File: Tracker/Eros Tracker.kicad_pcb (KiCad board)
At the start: 4 copper layers, 50 x 50 mm, 57 parts, among them J1 2171790001, J2 S8B-PH-SM4-TB(LF)(SN), J3 S2B-PH-SM4-TB(LF)(SN), J4 24881, J5 24881, J6 24881, J7 24881, M1 Motor_DC, Q1 NX138BKSX, Q2 NX138BKSX, Q3 DMP31D7LDW-7, Q4 DMP2240UDM-7, Q5 DMC1028UVT-7, Q6 DMC1028UVT-7, SW1 EVQ-P7A01P, U1 ESP32-C3-WROOM-02-N4, U2 TPS62A01A, U3 MCP73834-FCI/MF, U4 BNO086

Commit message: Alpha release
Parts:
- added G***: LOGO, LOGO, B.Cu at (164.9, 104.4)
- moved C3 67.0 mm to (179.1, 109.5), turned to 180 degrees
- moved R13 66.8 mm to (179.1, 114.7), turned to 180 degrees
- moved L1 66.5 mm to (179.0, 112.2), turned to 0 degrees
- moved C2 60.0 mm to (175.6, 109.5), turned to 0 degrees
- moved R14 59.6 mm to (175.5, 114.7), turned to 180 degrees
- moved U2 59.5 mm to (175.5, 112.2), turned to -90 degrees
- moved SW1 45.8 mm to (187.7, 94.6), turned to -90 degrees
- moved J1 42.0 mm to (186.0, 106.5), turned to 90 degrees
- moved R3 38.3 mm to (184.2, 98.6), turned to 180 degrees
- moved J3 36.0 mm to (147.0, 96.5)
- moved Q3 34.5 mm to (183.5, 95.6), turned to 90 degrees
- moved Q2 31.6 mm to (180.5, 95.6), turned to 90 degrees
- moved R23 30.2 mm to (180.0, 104.2), turned to 180 degrees
- moved R5 29.2 mm to (178.0, 95.6), turned to -90 degrees
- moved R22 29.2 mm to (179.0, 107.5), turned to 180 degrees
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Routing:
- net +BATT: track 6.89 -> 112.1 mm, vias 0 -> 4
- net Net-(LED1-A): track 0.00 -> 91.3 mm
- net /Eros Tracker Connectors/POWER_VIN1: track 0.00 -> 72.2 mm, vias 0 -> 4
- net /Eros Tracker BNO086 IMU/~{RESET}: track 0.00 -> 70.5 mm, vias 0 -> 4
- net GND: track 4.89 -> 67.5 mm, vias 1 -> 29
- net /Eros Tracker Connectors/VBUS: track 8.37 -> 67.6 mm, vias 0 -> 5
- net /Eros Tracker Connectors/POWER_VIN2: track 0.00 -> 58.8 mm, vias 0 -> 2
- net /Eros Tracker Power & Battery/~{BAT_STAT_CHARGING}: track 2.19 -> 42.0 mm, vias 0 -> 2
- net /Eros Tracker BNO086 IMU/I2C_SCL: track 3.34 -> 41.5 mm, vias 0 -> 2
- net /Eros Tracker Microcontroller/TACT_MOTOR0: track 0.00 -> 34.1 mm, vias 0 -> 2
- net /Eros Tracker Connectors/INT: track 0.00 -> 30.4 mm, vias 0 -> 2
- net /Eros Tracker BNO086 IMU/I2C_SDA: track 3.34 -> 33.3 mm, vias 0 -> 2
- net +3V3: track 10.3 -> 36.7 mm, vias 3 -> 14
- net /Eros Tracker Microcontroller/ENABLE_LATCH: track 0.00 -> 26.0 mm, vias 0 -> 2
- net /Eros Tracker Microcontroller/TACT_MOTOR1: track 3.67 -> 27.8 mm, vias 0 -> 2
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- added copper zone on In2.Cu, net +3V3
- added copper zone on In1.Cu, net GND
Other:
- board text added: "0"
- board text added: "0 mm"
- board text added: "0.01 mm"
- board text added: "0.02"
- board text added: "0.035 mm"
- board text added: "0.0900 mm / 0.0900 mm"
- board text added: "0.1 mm"
- board text added: "0.2500 mm"
- board text added: "1"
- board text added: "1.64 mm"
- board text added: "2.0000 mm"
- board text added: "3.3"
- board text added: "4"
- board text added: "4.5"
- board text added: "50.0000 mm x 50.0000 mm"
- board text added: "B.Cu"
- board text added: "B.Mask"
- board text added: "B.Paste"
- board text added: "B.Silkscreen"
- board text added: "BOARD CHARACTERISTICS"
- board text added: "Board Thickness:"
- board text added: "Board overall dimensions:"
- board text added: "Bottom Silk Screen"
- board text added: "Bottom Solder Mask"
- board text added: "Bottom Solder Paste"
- board text added: "Castellated pads:"
- board text added: "Color"
- board text added: "Copper Finish:"
- board text added: "Copper Layer Count:"
- board text added: "Dielectric 1"
- board text added: "Dielectric 2"
- board text added: "Dielectric 3"
- board text added: "Edge card connectors:"
- board text added: "Epsilon R"
- board text added: "F.Cu"
- board text added: "F.Mask"
- board text added: "F.Paste"
- board text added: "F.Silkscreen"
- board text added: "FR4"
- board text added: "Impedance Control:"
- board text added: "In1.Cu"
- board text added: "In2.Cu"
- board text added: "JLCJLCJLCJLC"
- board text added: "Layer Name"
- board text added: "Loss Tangent"
- board text added: "Material"
- board text added: "Min hole diameter:"
- board text added: "Min track/spacing:"
- board text added: "No"
- board text added: "None"
- board text added: "Not specified"
- board text added: "Plated Board Edge:"
- board text added: "Thickness (mm)"
- board text added: "Top Silk Screen"
- board text added: "Top Solder Mask"
- board text added: "Top Solder Paste"
- board text added: "Type"
- board text added: "copper"
- board text added: "core"
- board text added: "prepreg"

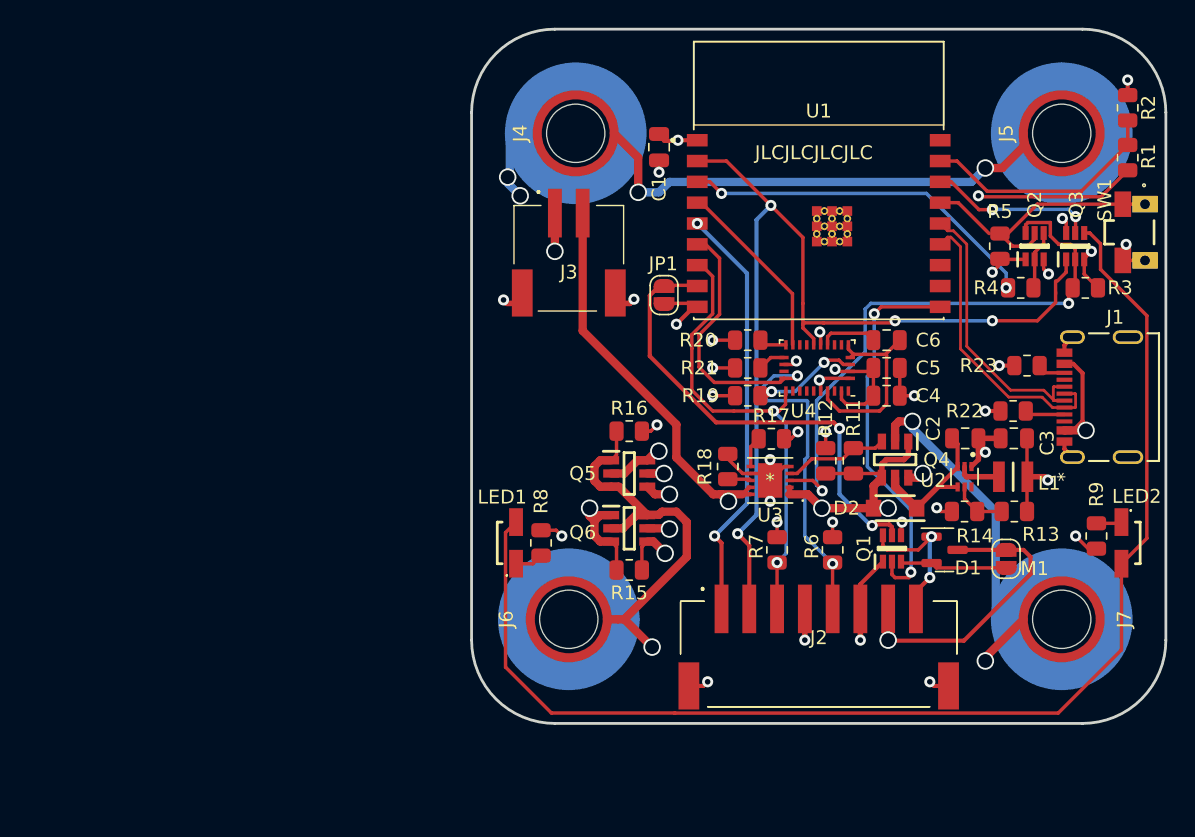
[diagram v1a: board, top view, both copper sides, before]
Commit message: RevC release. Power passthrough, battery voltage monitoring, IMU interrupt line fixed. TVS diodes added to all human-reachable connections.
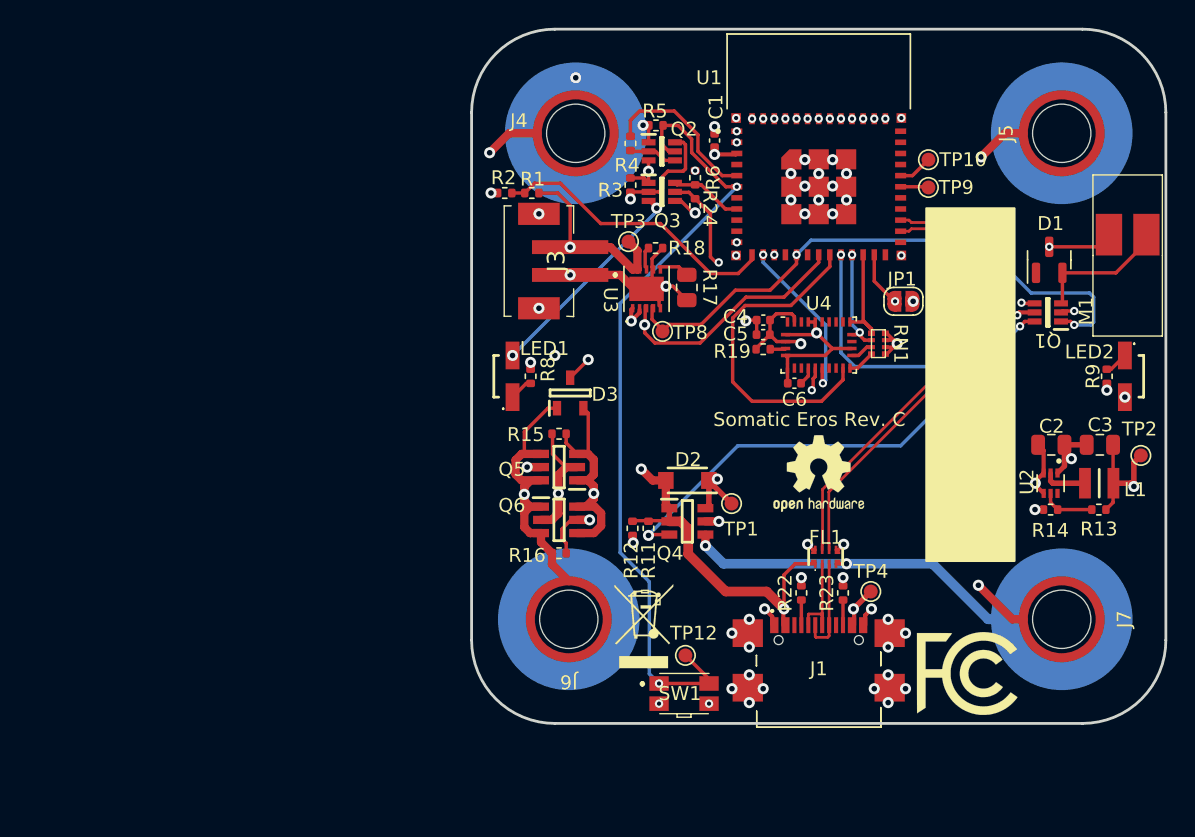
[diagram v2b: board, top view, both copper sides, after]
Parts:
- removed J2: S8B-PH-SM4-TB(LF)(SN), Eros Tracker:S8BPHSM4TBLFSN
- removed R20, R21, R7: 2.2k, Resistor_SMD:R_0805_2012Metric
- added D3: PESD5V2S2UT,215, Eros Tracker:SOT95P230X110-3N, F.Cu at (147.1, 106.2)
- added FL1: ECMF02-4CMX8, Eros Tracker:ECMF024CMX8, F.Cu at (165.5, 118.0)
- added R24: 10k 1%, Resistor_SMD:R_0402_1005Metric, F.Cu at (156.1, 92.7)
- added REF**: FCC-Logo_7.3x6mm_SilkScreen, Symbol:FCC-Logo_7.3x6mm_SilkScreen, F.Cu at (175.7, 126.4)
- added REF**: WEEE-Logo_4.2x6mm_SilkScreen, Symbol:WEEE-Logo_4.2x6mm_SilkScreen, F.Cu at (152.4, 123.0)
- added REF**: OSHW-Logo2_7.3x6mm_SilkScreen, Symbol:OSHW-Logo2_7.3x6mm_SilkScreen, F.Cu at (165.0, 112.0)
- added RN1: 2.2k, Eros Tracker:CAY10-xxxJ4, F.Cu at (169.3, 102.7)
- added TP1: TestPoint, TestPoint:TestPoint_Pad_D1.0mm, F.Cu at (158.7, 114.2)
- added TP10: TestPoint, TestPoint:TestPoint_Pad_D1.0mm, F.Cu at (172.9, 89.4)
- added TP12: TestPoint, TestPoint:TestPoint_Pad_D1.0mm, F.Cu at (155.4, 125.1)
- added TP2: TestPoint, TestPoint:TestPoint_Pad_D1.0mm, F.Cu at (188.2, 110.7)
- added TP3: TestPoint, TestPoint:TestPoint_Pad_D1.0mm, F.Cu at (151.3, 95.3)
- added TP4: TestPoint, TestPoint:TestPoint_Pad_D1.0mm, F.Cu at (168.8, 120.5)
- added TP8: TestPoint, TestPoint:TestPoint_Pad_D1.0mm, F.Cu at (153.8, 101.8)
- added TP9: TestPoint, TestPoint:TestPoint_Pad_D1.0mm, F.Cu at (172.9, 91.4)
- C1, C4, C5, C6: footprint Capacitor_SMD:C_0805_2012Metric -> Capacitor_SMD:C_0402_1005Metric
- J1: value 2171790001 -> USB4110-GF-A; footprint Eros Tracker:2171790001_MOL -> Eros Tracker:USB4110GFA
- J3: value S2B-PH-SM4-TB(LF)(SN) -> B2B-PH-SM4-TB(LF)(SN); footprint Eros Tracker:S2BPHSM4TBLFSN -> Eros Tracker:B2BPHSM4TBLFSN
- LOGO: renamed from G***; footprint LOGO -> Eros Tracker:SomaticLogo
- M1: value Motor_DC -> LCM04084521-B1; footprint Jumper:SolderJumper-2_P1.3mm_Open_RoundedPad1.0x1.5mm -> Eros Tracker:LCM04084521-B1
- R1, R11, R12, R13, R14, R15, R16, R18, R19, R2, R22, R23, R3, R4, R5, R8, R9: footprint Resistor_SMD:R_0805_2012Metric -> Resistor_SMD:R_0402_1005Metric
- R6: value 2.2k -> 100k; footprint Resistor_SMD:R_0805_2012Metric -> Resistor_SMD:R_0402_1005Metric
- SW1: footprint Eros Tracker:EVQ-9P701P -> Eros Tracker:EVQ-P7J01P
- U1: value ESP32-C3-WROOM-02-N4 -> ESP32-C3-MINI-1-N4; footprint Eros Tracker:ESP32-C3-WROOM-02-N4-MODULE_ESP32-C3-WROOM-02-H4 -> Eros Tracker:XCVR_ESP32-C3-MINI-1-N4
- moved SW1 46.6 mm to (155.0, 127.8), turned to 0 degrees
- moved R2 45.3 mm to (142.4, 91.8), turned to 180 degrees
- moved R1 43.0 mm to (144.3, 91.8), turned to 180 degrees
- moved R3 33.6 mm to (151.4, 91.2), turned to -90 degrees
- moved Q3 30.0 mm to (153.7, 91.7), turned to 0 degrees
- moved R4 30.0 mm to (151.4, 88.2), turned to -90 degrees
- moved J1 29.1 mm to (165.0, 126.6), turned to 0 degrees
- moved R6 28.6 mm to (156.1, 90.7), turned to 90 degrees
- moved Q2 27.7 mm to (153.7, 88.8), turned to 0 degrees
- moved R5 26.3 mm to (153.3, 86.9), turned to 180 degrees
- moved M1 23.5 mm to (187.2, 96.3), turned to 90 degrees
- moved D1 22.2 mm to (181.6, 96.6), turned to 90 degrees
- moved R23 21.1 mm to (166.8, 120.6), turned to 90 degrees
- moved Q1 20.4 mm to (181.5, 100.4), turned to 180 degrees
- moved R22 20.1 mm to (163.8, 120.6), turned to 90 degrees
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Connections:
- C6 pad 2: Net-(U4-PS0/WAKE) -> GND
- D1 pad 1: /Eros Tracker Connectors/-EXT_MOTOR -> unconnected-(D1-Pad1)
- J1 pad A6: /Eros Tracker Connectors/USB_D+ -> Net-(FL1-D+_1)
- J1 pad A7: /Eros Tracker Connectors/USB_D- -> Net-(FL1-D-_1)
- J1 pad B6: /Eros Tracker Connectors/USB_D+ -> Net-(FL1-D+_1)
- J1 pad B7: /Eros Tracker Connectors/USB_D- -> Net-(FL1-D-_1)
- JP1 pad 2: /Eros Tracker Microcontroller/TACT_MOTOR0 -> /Eros Tracker Microcontroller/~{LED}
- Q1 pad 1: GND -> /Eros Tracker Microcontroller/~{BAT_STAT_CHRG_DONE}
- Q1 pad 2: /Eros Tracker Microcontroller/TACT_MOTOR1 -> +3V3
- Q1 pad 5: /Eros Tracker Microcontroller/TACT_MOTOR0 -> /Eros Tracker Microcontroller/TACT_MOTOR
- Q1 pad 6: /Eros Tracker Connectors/-EXT_MOTOR -> Net-(Q1A-D1)
- Q2 pad 6: /Eros Tracker Power & Battery/~{BAT_STAT_CHARGING} -> /Eros Tracker Microcontroller/~{BAT_STAT_CHARGING}
- Q3 pad 1: /Eros Tracker BNO086 IMU/~{RESET} -> +3V3
- Q3 pad 2: /Eros Tracker Power & Battery/~{BAT_STAT_CHARGING} -> /Eros Tracker Microcontroller/~{BAT_STAT_CHARGING}
- Q3 pad 3: +3V3 -> Net-(LED1-A)
- Q3 pad 4: Net-(LED1-A) -> +3V3
- Q3 pad 6: +3V3 -> /Eros Tracker Microcontroller/MCU_ENABLE
- Q4 pad 2: /Eros Tracker Connectors/VBUS_OUT -> /Eros Tracker Connectors/VBUS
- Q4 pad 3: /Eros Tracker Power & Battery/~{BAT_STAT_CHRG_DONE} -> Net-(Q1A-D1)
- Q4 pad 4: /Eros Tracker Connectors/VBUS -> /Eros Tracker Connectors/VBUS_OUT
- Q4 pad 5: /Eros Tracker Power & Battery/VIN -> +BATT
- Q4 pad 6: +BATT -> /Eros Tracker Power & Battery/VIN
- Q5 pad 2: /Eros Tracker Connectors/POWER_VIN1 -> /Eros Tracker Connectors/VBUS
- Q5 pad 4: /Eros Tracker Connectors/VBUS -> /Eros Tracker Connectors/POWER_VIN1
- Q6 pad 2: /Eros Tracker Connectors/POWER_VIN2 -> /Eros Tracker Connectors/VBUS
- Q6 pad 4: /Eros Tracker Connectors/VBUS -> /Eros Tracker Connectors/POWER_VIN2
- R1 pad 2: Net-(U1-IO1) -> /Eros Tracker Microcontroller/ADC_BATT_V
- R11 pad 2: /Eros Tracker Power & Battery/~{BAT_STAT_CHRG_DONE} -> Net-(Q1A-D1)
- R2 pad 1: Net-(U1-IO1) -> /Eros Tracker Microcontroller/ADC_BATT_V
- R3 pad 2: /Eros Tracker Power & Battery/~{BAT_STAT_CHARGING} -> /Eros Tracker Microcontroller/~{BAT_STAT_CHARGING}
- R6 pad 1: +3V3 -> /Eros Tracker Microcontroller/MCU_ENABLE
- R6 pad 2: /Eros Tracker BNO086 IMU/I2C_SCL -> GND
- U1 pad 1: +3V3 -> GND
- U1 pad 10: /Eros Tracker Microcontroller/TACT_MOTOR1 -> unconnected-(U1-NC-Pad10)
- U1 pad 11: unconnected-(U1-RXD-Pad11) -> GND
- U1 pad 12: unconnected-(U1-TXD-Pad12) -> /Eros Tracker Microcontroller/ADC_BATT_V
- U1 pad 13: /Eros Tracker Connectors/USB_D- -> /Eros Tracker BNO086 IMU/~{RESET}
- U1 pad 14: /Eros Tracker Connectors/USB_D+ -> GND
- U1 pad 15: /Eros Tracker Microcontroller/~{BUTTON_INPUT} -> unconnected-(U1-NC-Pad15)
- U1 pad 16: /Eros Tracker Microcontroller/~{LED} -> /Eros Tracker Microcontroller/~{BAT_STAT_CHRG_DONE}
- U1 pad 17: Net-(U1-IO1) -> unconnected-(U1-NC-Pad17)
- U1 pad 18: unconnected-(U1-IO0-Pad18) -> /Eros Tracker Microcontroller/~{BAT_STAT_CHARGING}
- U1 pad 19: GND -> /Eros Tracker BNO086 IMU/INT
- U1 pad 2: /Eros Tracker BNO086 IMU/~{RESET} -> GND
- U1 pad 20: GND -> /Eros Tracker Microcontroller/TACT_MOTOR
- U1 pad 21: GND -> /Eros Tracker BNO086 IMU/I2C_SCL
- U1 pad 22: GND -> /Eros Tracker BNO086 IMU/I2C_SDA
- U1 pad 23: GND -> /Eros Tracker Microcontroller/~{LED}
- U1 pad 24: GND -> unconnected-(U1-NC-Pad24)
- U1 pad 25: GND -> unconnected-(U1-NC-Pad25)
- U1 pad 26: GND -> /Eros Tracker Connectors/USB_D-
- U1 pad 27: GND -> /Eros Tracker Connectors/USB_D+
- U1 pad 28: GND -> unconnected-(U1-NC-Pad28)
- U1 pad 29: GND -> unconnected-(U1-NC-Pad29)
- U1 pad 3: /Eros Tracker Microcontroller/ENABLE_LATCH -> +3V3
- U1 pad 30: GND -> Net-(U1-RXD0)
- U1 pad 31: GND -> Net-(U1-TXD0)
- U1 pad 32: GND -> unconnected-(U1-NC-Pad32)
- U1 pad 33: GND -> unconnected-(U1-NC-Pad33)
- U1 pad 34: GND -> unconnected-(U1-NC-Pad34)
- U1 pad 35: GND -> unconnected-(U1-NC-Pad35)
- U1 pad 4: /Eros Tracker BNO086 IMU/INT -> unconnected-(U1-NC-Pad4)
- U1 pad 5: /Eros Tracker Connectors/INT -> /Eros Tracker Microcontroller/ENABLE_LATCH
- U1 pad 6: /Eros Tracker BNO086 IMU/I2C_SCL -> /Eros Tracker Microcontroller/~{BUTTON_INPUT}
- U1 pad 7: /Eros Tracker BNO086 IMU/I2C_SDA -> unconnected-(U1-NC-Pad7)
- U1 pad 8: /Eros Tracker Microcontroller/TACT_MOTOR0 -> /Eros Tracker Microcontroller/MCU_ENABLE
- U1 pad 9: GND -> unconnected-(U1-NC-Pad9)
- U3 pad 3: /Eros Tracker Power & Battery/~{BAT_STAT_CHARGING} -> /Eros Tracker Microcontroller/~{BAT_STAT_CHARGING}
- U3 pad 4: /Eros Tracker Power & Battery/~{BAT_STAT_CHRG_DONE} -> /Eros Tracker Microcontroller/~{BAT_STAT_CHRG_DONE}
- U4 pad 26: Net-(U4-PS0/WAKE) -> GND
- U4 pad 5: Net-(U4-PS0/WAKE) -> GND
- U4 pad 6: Net-(U4-PS0/WAKE) -> GND
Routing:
- net /Eros Tracker BNO086 IMU/~{RESET}: track 70.5 -> 12.3 mm, vias 4 -> 2
- net /Eros Tracker Microcontroller/~{BAT_STAT_CHRG_DONE}: track 0.00 -> 42.3 mm, vias 0 -> 2
- net /Eros Tracker Power & Battery/~{BAT_STAT_CHARGING}: track 42.0 -> 0.00 mm, vias 2 -> 0
- net /Eros Tracker Microcontroller/~{BUTTON_INPUT}: track 19.3 -> 57.0 mm, vias 0 -> 2
- net Net-(Q1A-D1): track 0.00 -> 35.7 mm, vias 0 -> 2
- net /Eros Tracker Microcontroller/~{BAT_STAT_CHARGING}: track 0.00 -> 35.5 mm, vias 0 -> 2
- net Net-(LED1-A): track 91.3 -> 56.9 mm, vias 0 -> 3
- net /Eros Tracker BNO086 IMU/I2C_SCL: track 41.5 -> 7.40 mm
- net /Eros Tracker Microcontroller/TACT_MOTOR0: track 34.1 -> 0.00 mm, vias 2 -> 0
- net /Eros Tracker Connectors/INT: track 30.4 -> 0.00 mm, vias 2 -> 0
- net +BATT: track 112.1 -> 83.1 mm, vias 4 -> 3
- net /Eros Tracker Microcontroller/TACT_MOTOR1: track 27.8 -> 0.00 mm, vias 2 -> 0
- net /Eros Tracker BNO086 IMU/I2C_SDA: track 33.3 -> 7.66 mm, vias 2 -> 0
- net /Eros Tracker Connectors/POWER_VIN1: track 72.2 -> 96.4 mm
- net /Eros Tracker Microcontroller/TACT_MOTOR: track 0.00 -> 23.0 mm, vias 0 -> 2
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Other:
- board text added: "Somatic Eros Rev. C"
- board text removed: "JLCJLCJLCJLC"
